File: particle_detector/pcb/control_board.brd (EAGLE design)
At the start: 64 x 32 mm, 30 parts, among them IC1 LT1807R, IC3 LT3461, IC4 TEENSY 3.2

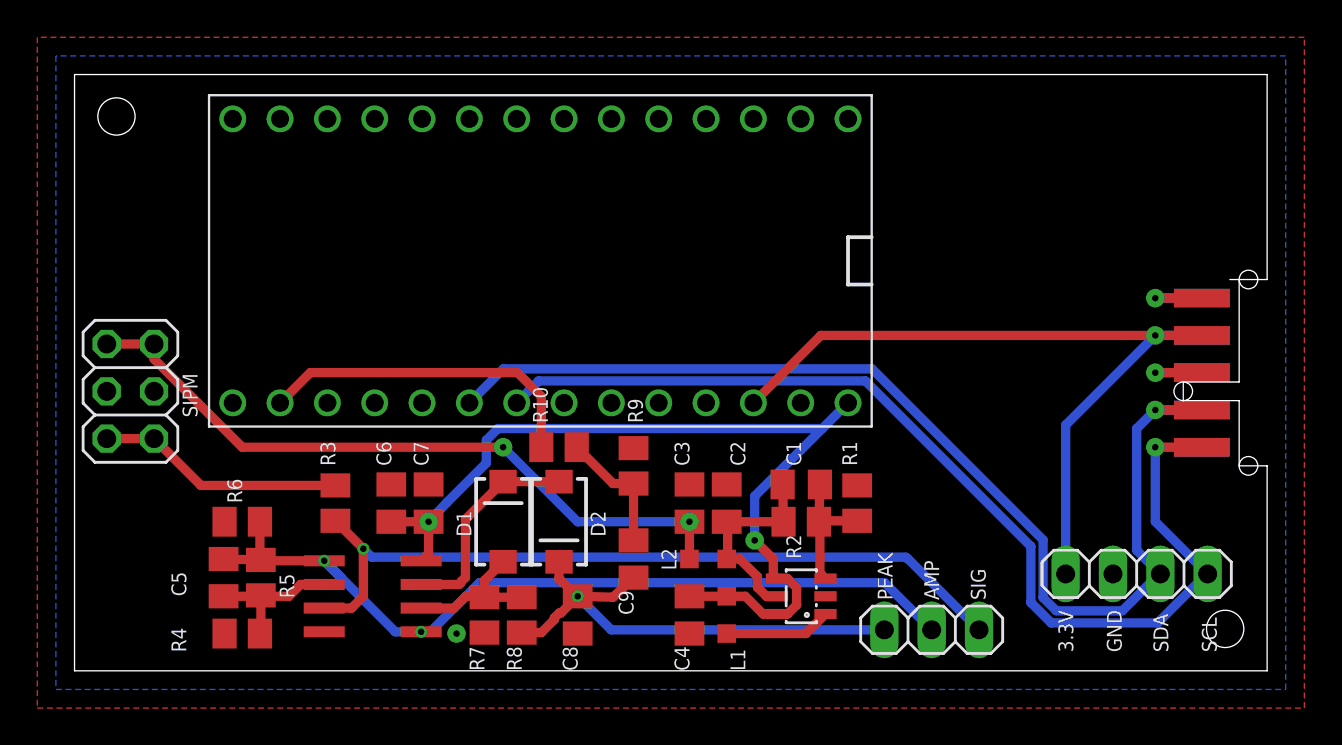
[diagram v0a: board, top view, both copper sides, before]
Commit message: fix AGNd and 3.3V issue; needs DRC
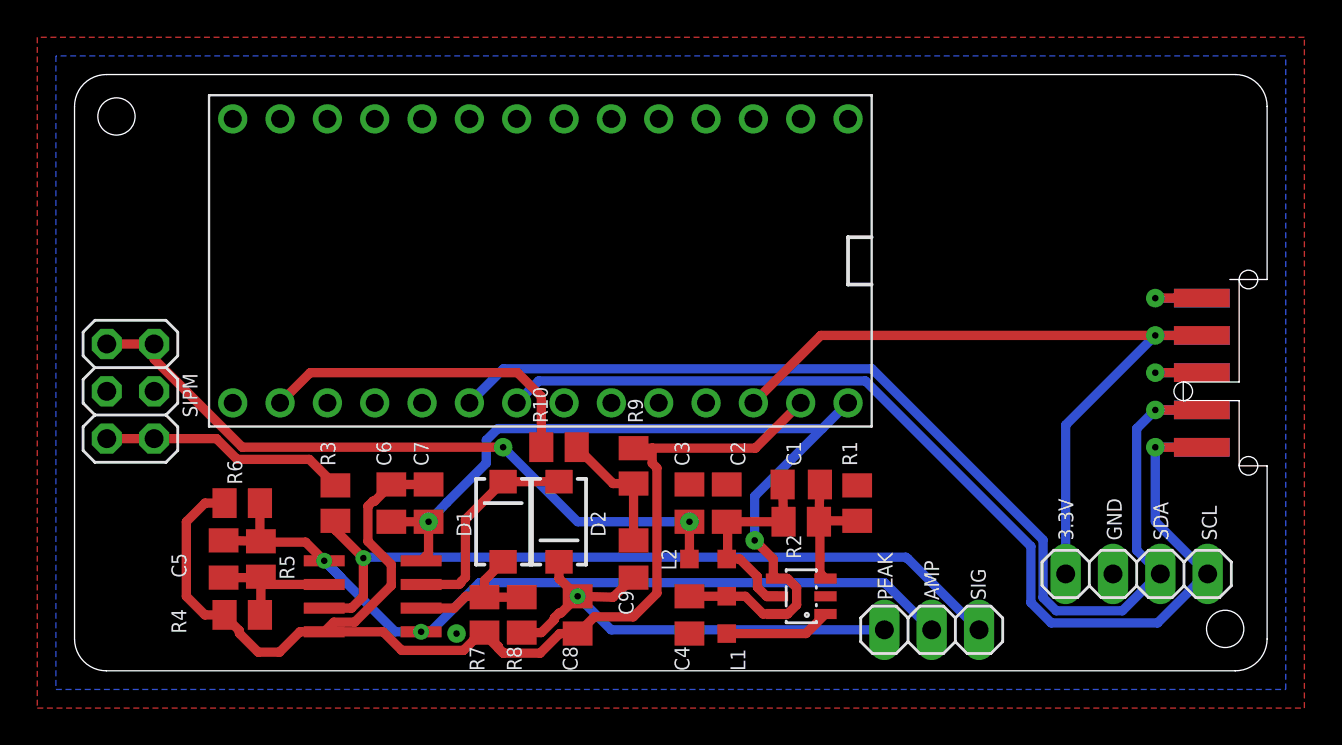
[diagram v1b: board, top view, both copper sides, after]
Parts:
- moved C5 1.00 mm to (34.0, 6.00)
- moved R4 1.00 mm to (35.0, 3.00)
- moved R5 1.00 mm to (36.0, 6.00)
- moved R6 1.00 mm to (35.0, 9.00)
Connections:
- net AGND: now also C6.2, C7.2, C8.2, IC1.4, R4.1, R6.1, R7.1, R9.1
- net GND: no longer C6.2, C7.2, C8.2, IC1.4, R4.1, R6.1, R7.1, R9.1
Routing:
- net AGND: track 0.00 -> 68.7 mm
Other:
- outline, holes or cut-outs redrawn
